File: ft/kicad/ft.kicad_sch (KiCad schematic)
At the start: 2 parts, among them J1 Conn_RIOT, J2 Conn_ft

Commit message: Change ft interface connector to IDC type
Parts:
- J2: footprint Connector_PinHeader_2.54mm:PinHeader_2x10_P2.54mm_Horizontal -> Connector_IDC:IDC-Header_2x10_P2.54mm_Horizontal
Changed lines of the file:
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@@
       (effects (font (size 1.27 1.27)))
     )
-    (property "Footprint" "Connector_PinHeader_2.54mm:PinHeader_2x10_P2.54mm_Horizontal" (at 142.24 66.04 0)
+    (property "Footprint" "Connector_IDC:IDC-Header_2x10_P2.54mm_Horizontal" (at 142.24 66.04 0)
       (effects (font (size 1.27 1.27)) hide)
     )

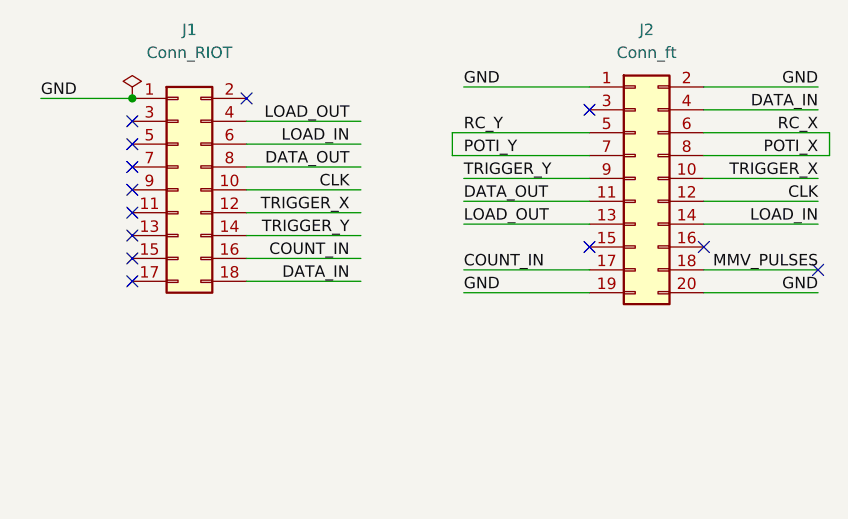
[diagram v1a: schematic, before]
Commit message: Add DATA_IN selection jumper
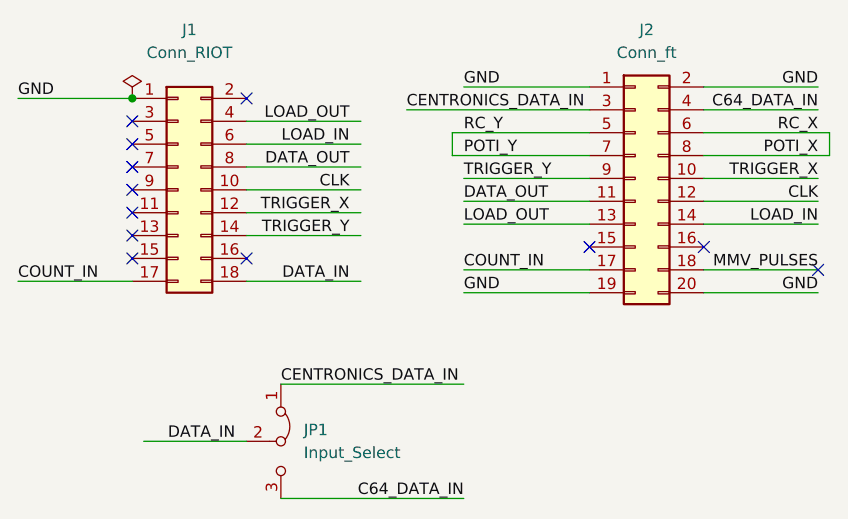
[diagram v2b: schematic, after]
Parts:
- added JP1: Input_Select, Connector_PinHeader_2.54mm:PinHeader_1x03_P2.54mm_Vertical, symbol Jumper:Jumper_3_Bridged12
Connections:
- net COUNT_IN: now also J1.17 (Pin_17); no longer J1.16 (Pin_16)
- net DATA_IN: now also JP1.2 (C); no longer J2.4 (Pin_4)
- net CENTRONICS_DATA_IN: now reaches J2.3 (Pin_3)
- net CENTRONICS_DATA_IN: now also JP1.1 (A)
- new net C64_DATA_IN: J2.4 (Pin_4), JP1.3 (B)
- no-connect marks 13 -> 12
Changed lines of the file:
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@@
   (junction (at 86.36 57.15) (diameter 0) (color 0 0 0 0)
   )
-  (no_connect (at 99.06 57.15))
   (no_connect (at 86.36 59.69))
   (no_connect (at 162.56 76.2))
   (no_connect (at 86.36 64.77))
-  (no_connect (at 137.16 58.42))
   (no_connect (at 86.36 72.39))
+  (no_connect (at 99.06 57.15))
   (no_connect (at 86.36 74.93))
-  (no_connect (at 86.36 77.47))
+  (no_connect (at 99.06 74.93))
   (no_connect (at 86.36 62.23))
   (no_connect (at 86.36 67.31))
@@
     (stroke (width 0) (type default))
   )
+  (wire (pts (xy 73.66 57.15) (xy 86.36 57.15))
+    (stroke (width 0) (type default))
+  )
   (wire (pts (xy 111.76 62.23) (xy 99.06 62.23))
     (stroke (width 0) (type default))
@@
     (stroke (width 0) (type default))
   )
-  (wire (pts (xy 86.36 57.15) (xy 76.2 57.15))
-    (stroke (width 0) (type default))
-  )
   (wire (pts (xy 111.76 64.77) (xy 99.06 64.77))
     (stroke (width 0) (type default))
   )
+  (wire (pts (xy 99.06 95.25) (xy 87.63 95.25))
+    (stroke (width 0) (type default))
+  )
+  (wire (pts (xy 116.84 58.42) (xy 137.16 58.42))
+    (stroke (width 0) (type default))
+  )
   (wire (pts (xy 163.83 60.96) (xy 149.86 60.96))
     (stroke (width 0) (type default))
   )
+  (wire (pts (xy 73.66 77.47) (xy 86.36 77.47))
+    (stroke (width 0) (type default))
+  )
   (wire (pts (xy 111.76 77.47) (xy 99.06 77.47))
     (stroke (width 0) (type default))
@@
     (stroke (width 0) (type default))
   )
+  (wire (pts (xy 102.87 88.9) (xy 123.19 88.9))
+    (stroke (width 0) (type default))
+  )
   (wire (pts (xy 163.83 63.5) (xy 149.86 63.5))
     (stroke (width 0) (type default))
@@
     (stroke (width 0) (type default))
   )
+  (wire (pts (xy 123.19 101.6) (xy 102.87 101.6))
+    (stroke (width 0) (type default))
+  )
   (wire (pts (xy 137.16 66.04) (xy 123.19 66.04))
     (stroke (width 0) (type default))
@@
     (stroke (width 0) (type default))
   )
-  (wire (pts (xy 111.76 74.93) (xy 99.06 74.93))
-    (stroke (width 0) (type default))
-  )
   (label "DATA_OUT" (at 110.49 64.77 180) (fields_autoplaced)
     (effects (font (size 1.27 1.27)) (justify right bottom))
@@
     (effects (font (size 1.27 1.27)) (justify right bottom))
   )
-  (label "DATA_IN" (at 162.56 58.42 180) (fields_autoplaced)
+  (label "CENTRONICS_DATA_IN" (at 102.87 88.9 0) (fields_autoplaced)
+    (effects (font (size 1.27 1.27)) (justify left bottom))
+  )
+  (label "C64_DATA_IN" (at 162.56 58.42 180) (fields_autoplaced)
     (effects (font (size 1.27 1.27)) (justify right bottom))
   )
@@
     (effects (font (size 1.27 1.27)) (justify left bottom))
   )
+  (label "CENTRONICS_DATA_IN" (at 116.84 58.42 0) (fields_autoplaced)
+    (effects (font (size 1.27 1.27)) (justify left bottom))
+  )
   (label "GND" (at 123.19 55.88 0) (fields_autoplaced)
     (effects (font (size 1.27 1.27)) (justify left bottom))
@@
     (effects (font (size 1.27 1.27)) (justify right bottom))
   )
-  (label "GND" (at 76.2 57.15 0) (fields_autoplaced)
+  (label "GND" (at 73.66 57.15 0) (fields_autoplaced)
     (effects (font (size 1.27 1.27)) (justify left bottom))
   )
@@
     (effects (font (size 1.27 1.27)) (justify left bottom))
   )
+  (label "DATA_IN" (at 97.79 95.25 180) (fields_autoplaced)
+    (effects (font (size 1.27 1.27)) (justify right bottom))
+  )
+  (label "COUNT_IN" (at 73.66 77.47 0) (fields_autoplaced)
+    (effects (font (size 1.27 1.27)) (justify left bottom))
+  )
   (label "GND" (at 162.56 78.74 180) (fields_autoplaced)
     (effects (font (size 1.27 1.27)) (justify right bottom))
@@
     (effects (font (size 1.27 1.27)) (justify right bottom))
   )
-  (label "COUNT_IN" (at 110.49 74.93 180) (fields_autoplaced)
+  (label "C64_DATA_IN" (at 123.19 101.6 180) (fields_autoplaced)
     (effects (font (size 1.27 1.27)) (justify right bottom))
   )
@@
         )
       )
+    )
+  )
+  (symbol (lib_id "Jumper:Jumper_3_Bridged12") (at 102.87 95.25 270) (unit 1)
+    (in_bom yes) (on_board yes) (dnp no) (fields_autoplaced)
+    (property "Reference" "JP1" (at 105.41 93.98 90)
+      (effects (font (size 1.27 1.27)) (justify left))
+    )
+    (property "Value" "Input_Select" (at 105.41 96.52 90)
+      (effects (font (size 1.27 1.27)) (justify left))
+    )
+    (property "Footprint" "Connector_PinHeader_2.54mm:PinHeader_1x03_P2.54mm_Vertical" (at 102.87 95.25 0)
+      (effects (font (size 1.27 1.27)) hide)
+    )
+    (property "Datasheet" "~" (at 102.87 95.25 0)
+      (effects (font (size 1.27 1.27)) hide)
+    )
+    (pin "1")
+    (pin "2")
+    (pin "3")
+    (instances
+      (project "ft"
+        (path "/cd4fa989-0027-4df6-b169-965f38f1952c"
+          (reference "JP1") (unit 1)
+        )
+      )
